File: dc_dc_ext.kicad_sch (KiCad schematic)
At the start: 30 parts, among them U10 TPS56339DDC, U11 TPS56339DDC

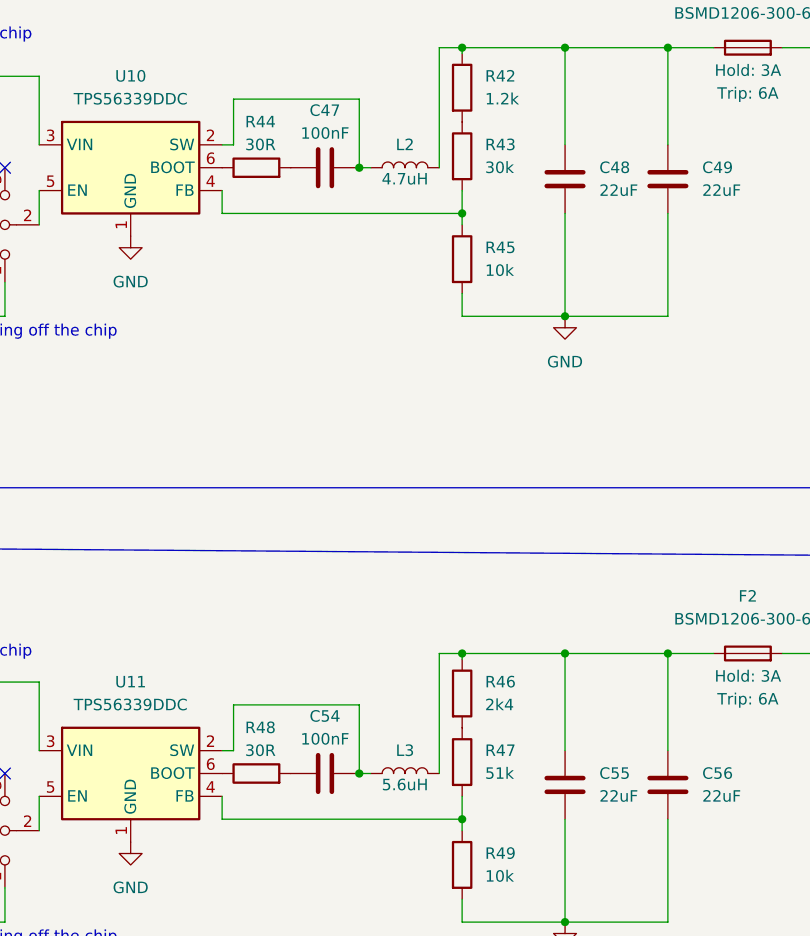
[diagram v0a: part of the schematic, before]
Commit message: Power circuit initial routing
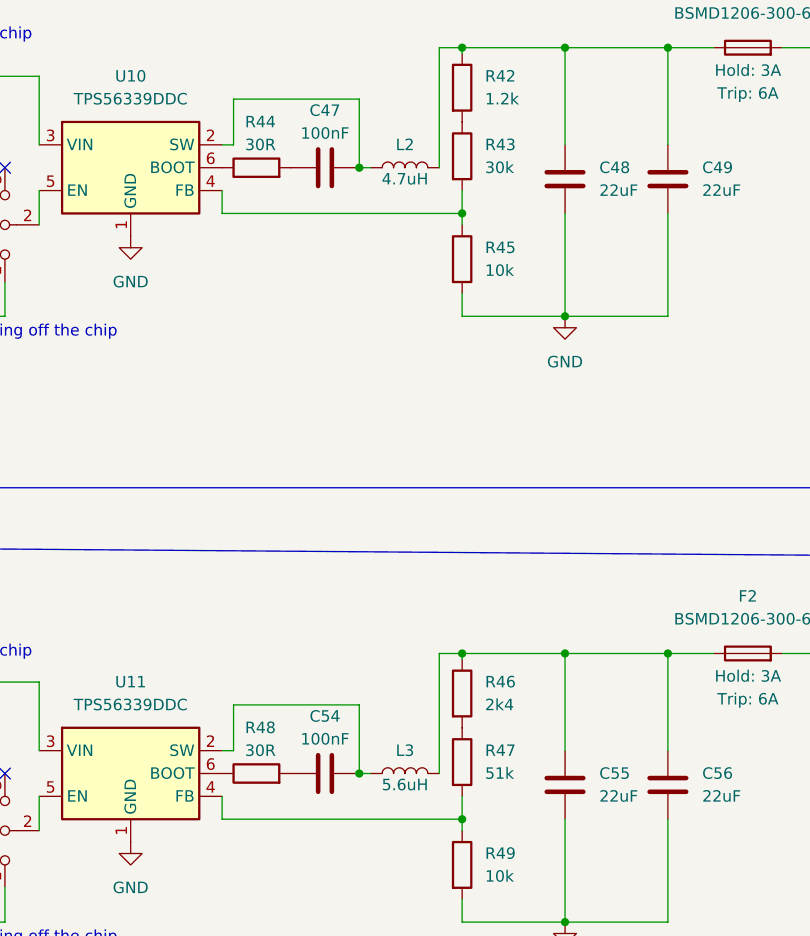
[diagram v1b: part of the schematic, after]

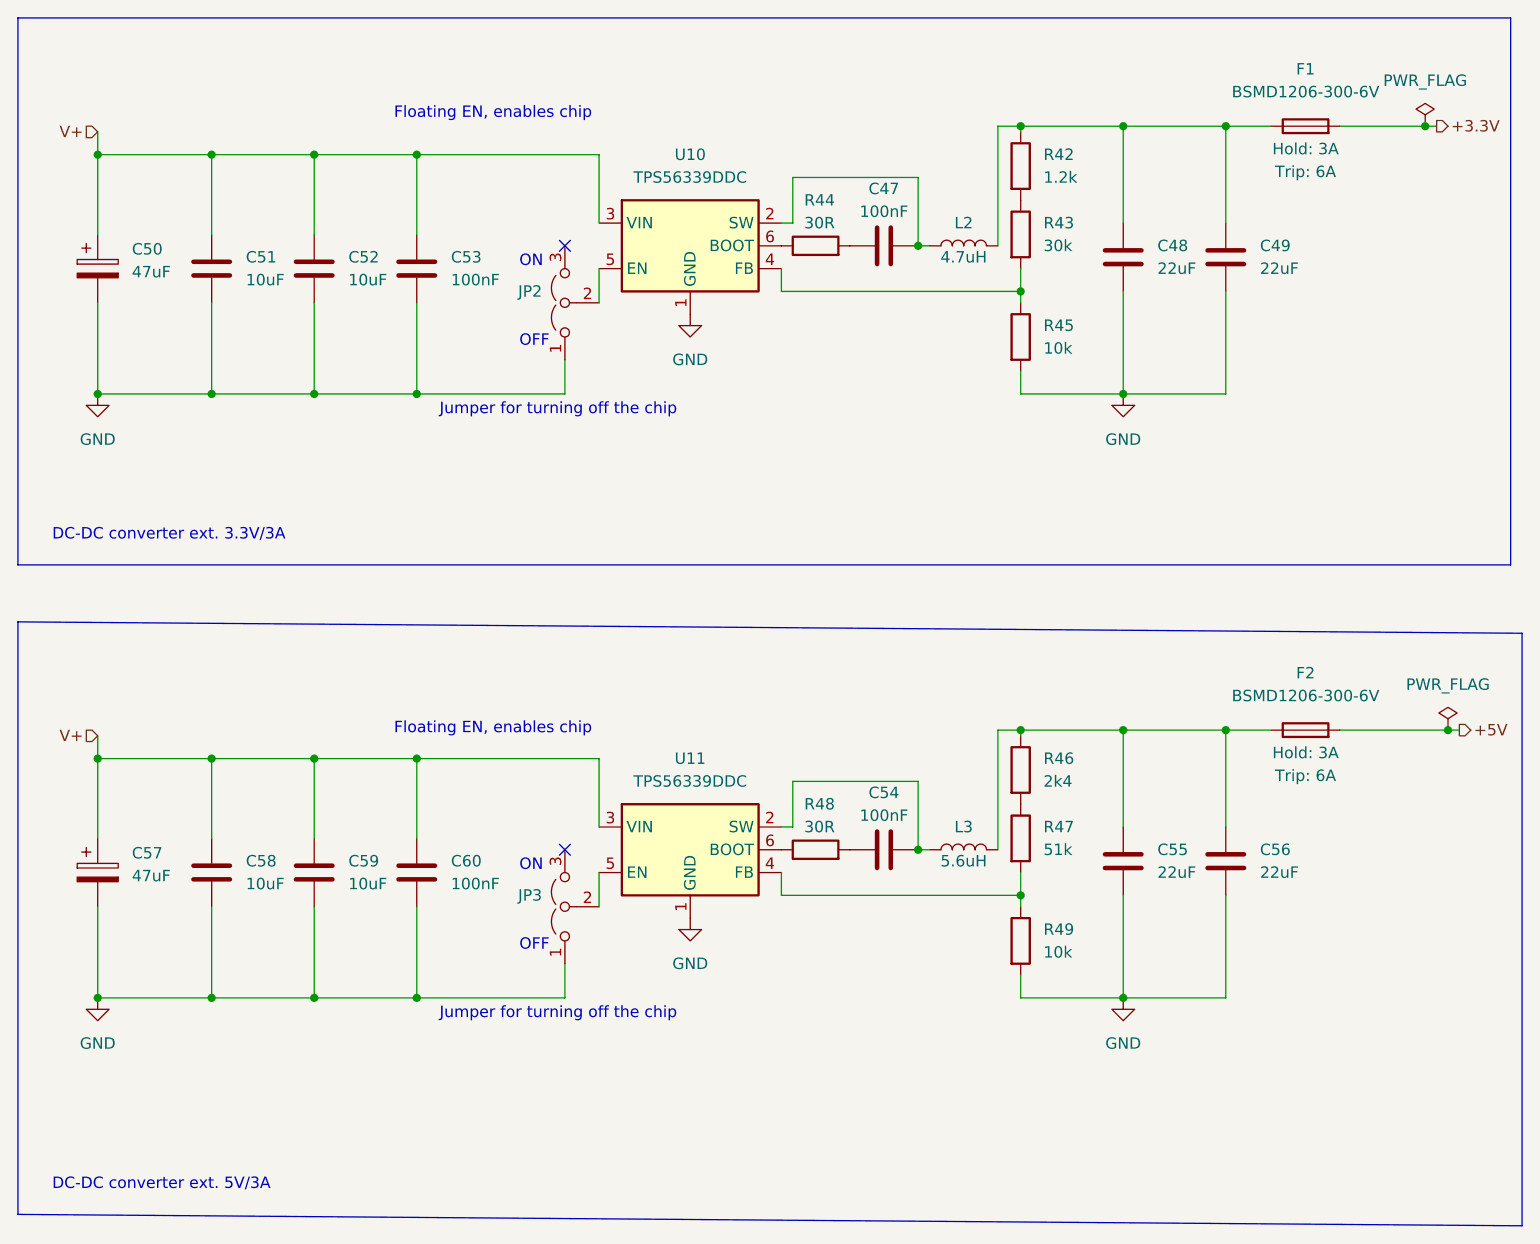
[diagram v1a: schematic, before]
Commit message: resolved align to grid warnings
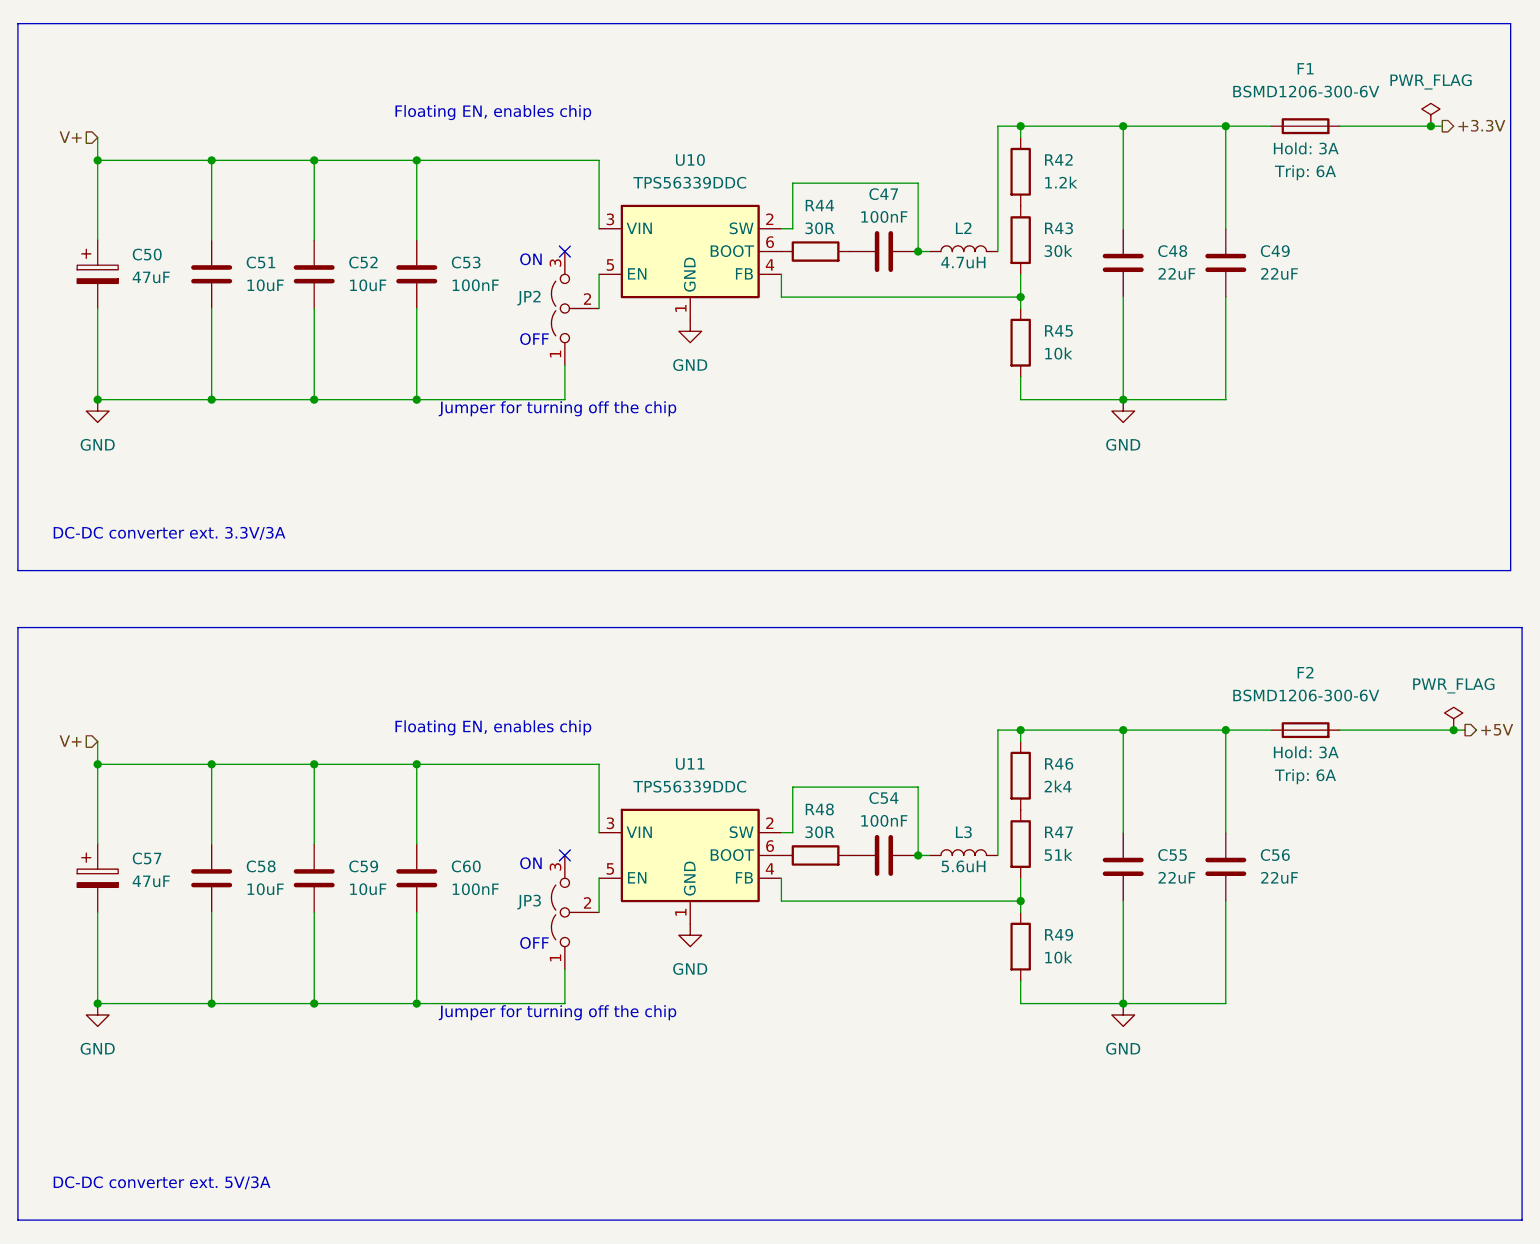
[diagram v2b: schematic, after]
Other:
- moved on the sheet: C47, C48, C49, C50, C51, C52, C53, C54, C55, C56, C57, C58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

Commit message: replaced 47uF caps due to supply shortage, rotation fix for 3535 adressable leds
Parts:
- C50, C57: LCSC Part C403725 -> C76659
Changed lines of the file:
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@@
       (effects (font (size 1.27 1.27)) hide)
     )
-    (property "Datasheet" "https://datasheet.lcsc.com/lcsc/1912111437_Murata-Electronics-GRM31CR61E476ME44L_C403725.pdf" (at 71.12 121.92 0)
+    (property "Datasheet" "https://datasheet.lcsc.com/lcsc/2304140030_TDK-C3216X5R1E476MTJ00E_C76659.pdf" (at 71.12 121.92 0)
       (effects (font (size 1.27 1.27)) hide)
     )
@@
       (effects (font (size 1.27 1.27)) hide)
     )
-    (property "LCSC Part" "C403725" (at 71.12 121.92 0)
+    (property "LCSC Part" "C76659" (at 71.12 121.92 0)
       (effects (font (size 1.27 1.27)) hide)
     )
@@
       (effects (font (size 1.27 1.27)) hide)
     )
-    (property "Datasheet" "https://datasheet.lcsc.com/lcsc/1912111437_Murata-Electronics-GRM31CR61E476ME44L_C403725.pdf" (at 71.12 54.61 0)
+    (property "Datasheet" "https://datasheet.lcsc.com/lcsc/2304140030_TDK-C3216X5R1E476MTJ00E_C76659.pdf" (at 71.12 54.61 0)
       (effects (font (size 1.27 1.27)) hide)
     )
@@
       (effects (font (size 1.27 1.27)) hide)
     )
-    (property "LCSC Part" "C403725" (at 71.12 54.61 0)
-      (effects (font (size 1.27 1.27)) hide)
-    )
+    (property "LCSC Part" "C76659" (at 71.12 54.61 0)
+      (effects (font (size 1.27 1.27)) hide)
+    )

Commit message: updated drawing corner, added license
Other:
- company: (none) -> University of Tartu
- title: (none) -> DC-DC converter for the MCU, LEDs, and external devices
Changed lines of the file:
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@@
 (kicad_sch (version 20230121) (generator eeschema)
   (paper "A4")
+  (title_block
+    (title "DC-DC converter for the MCU, LEDs, and external devices")
+    (date "2023-21-11")
+    (rev "0.2.0")
+    (company "University of Tartu")
+    (comment 1 "Licensed under CERN-OHL-P")
+  )
   (junction (at 173.99 57.15) (diameter 0) (color 0 0 0 0)
   )

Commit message: fixed i2c3_sda pin (from PA9 to PC9), excluding manual asm components from bom
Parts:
- JP2, JP3: now left out of the parts list
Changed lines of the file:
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@@
   )
   (symbol (lib_id "Jumper:Jumper_3_Open") (at 123.19 125.73 90) (unit 1)
-    (in_bom yes) (on_board yes) (dnp no) (fields_autoplaced)
+    (in_bom no) (on_board yes) (dnp no) (fields_autoplaced)
     (property "Reference" "JP3" (at 120.65 124.4599 90)
       (effects (font (size 1.27 1.27)) (justify left))
@@
   )
   (symbol (lib_id "Jumper:Jumper_3_Open") (at 123.19 58.42 90) (unit 1)
-    (in_bom yes) (on_board yes) (dnp no) (fields_autoplaced)
+    (in_bom no) (on_board yes) (dnp no) (fields_autoplaced)
     (property "Reference" "JP2" (at 120.65 57.1499 90)
       (effects (font (size 1.27 1.27)) (justify left))

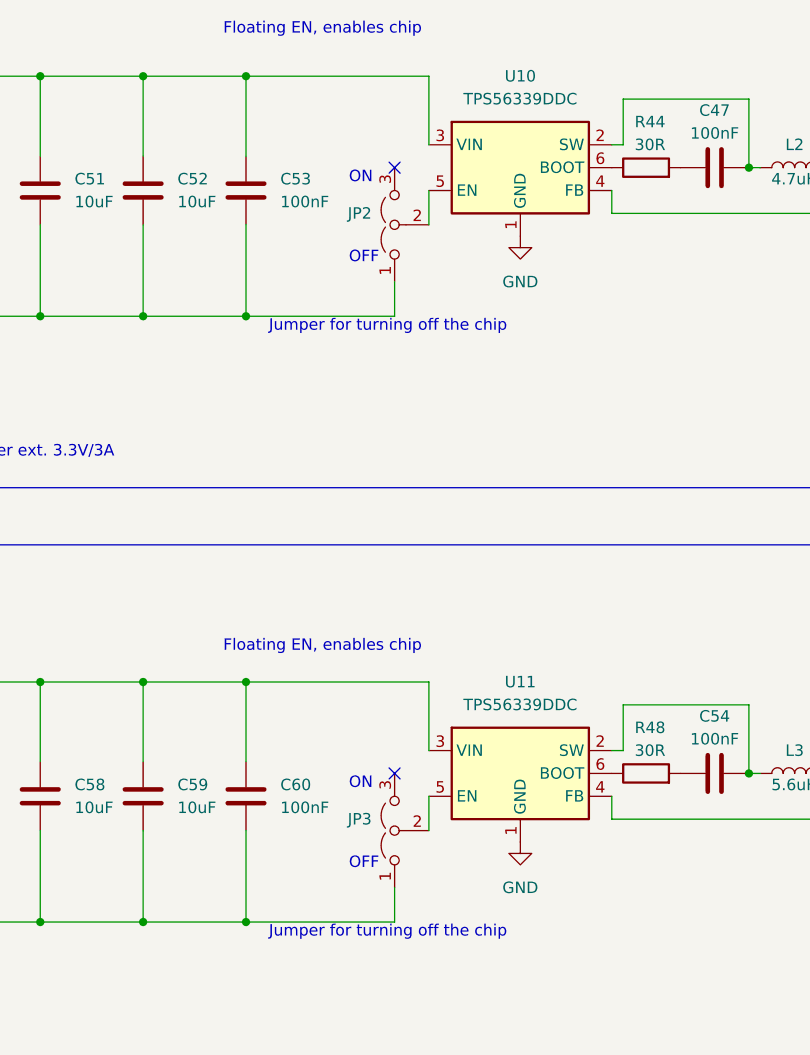
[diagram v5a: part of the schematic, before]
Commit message: setting 'do not populate' attribute for manually assembled components
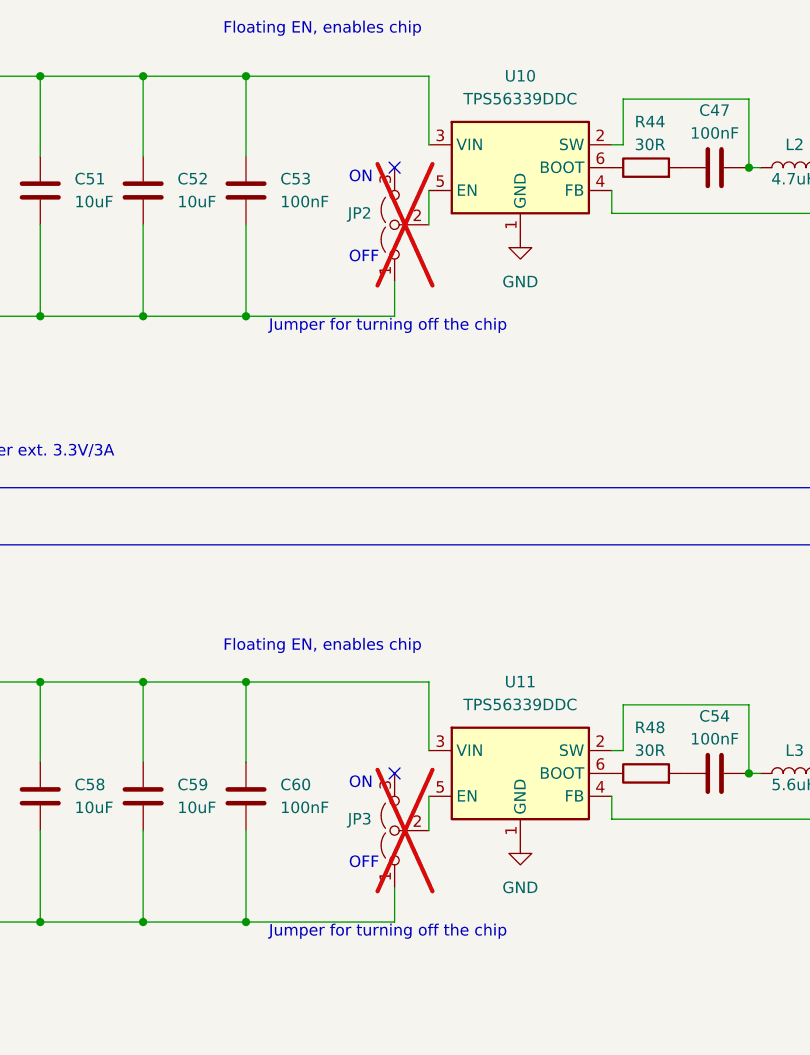
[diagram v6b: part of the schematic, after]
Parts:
- JP2, JP3: now not fitted; now in the parts list
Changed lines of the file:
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@@
   )
   (symbol (lib_id "Jumper:Jumper_3_Open") (at 123.19 125.73 90) (unit 1)
-    (in_bom no) (on_board yes) (dnp no) (fields_autoplaced)
+    (in_bom yes) (on_board yes) (dnp yes) (fields_autoplaced)
     (property "Reference" "JP3" (at 120.65 124.4599 90)
       (effects (font (size 1.27 1.27)) (justify left))
@@
   )
   (symbol (lib_id "Jumper:Jumper_3_Open") (at 123.19 58.42 90) (unit 1)
-    (in_bom no) (on_board yes) (dnp no) (fields_autoplaced)
+    (in_bom yes) (on_board yes) (dnp yes) (fields_autoplaced)
     (property "Reference" "JP2" (at 120.65 57.1499 90)
       (effects (font (size 1.27 1.27)) (justify left))
